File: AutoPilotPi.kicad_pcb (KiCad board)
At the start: 4 copper layers, 32.9 x 59.2 mm, 120 parts, among them J1 Conn_01x04_MountingPin, J2 Conn_01x03, J3 Conn_01x02, J4 USB_C_Receptacle, J5 Conn_01x03, J6 Conn_01x03, J7 Conn_01x03, M1 xr819, M2 mini_elrs, Q1 Q_NMOS_GSD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

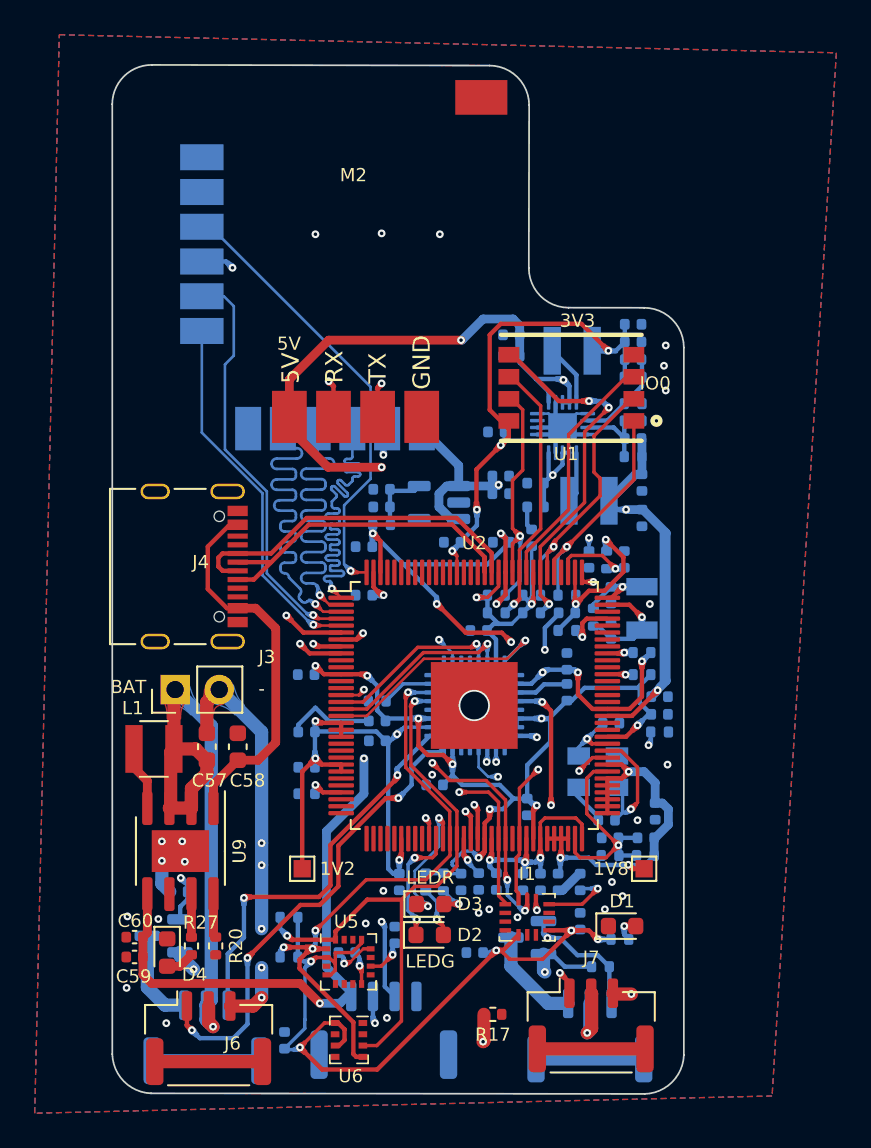
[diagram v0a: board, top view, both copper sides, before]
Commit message: add esp32 as wifi card
Signed-off-by: huangzzk <huangcmzzk@gmail.com>
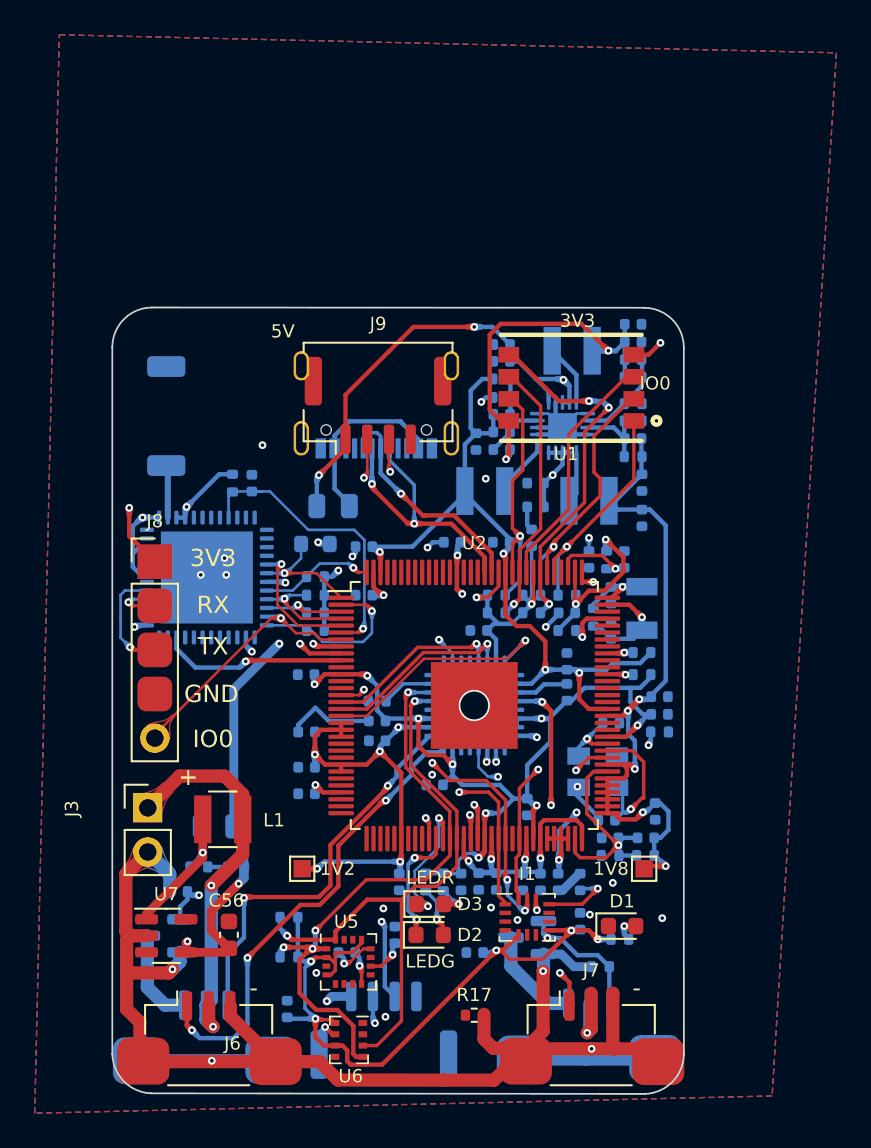
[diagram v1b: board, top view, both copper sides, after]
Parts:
- removed C59: 1u, Capacitor_SMD:C_0402_1005Metric
- removed C60: 0.1u, Capacitor_SMD:C_0402_1005Metric
- removed M1: xr819, ic_footprint:xr819_module
- removed M2: mini_elrs, ic_footprint:mini_elrs
- removed U9: ETA9640, Package_SO:SOIC-8-1EP_3.9x4.9mm_P1.27mm_EP2.41x3.3mm
- added AE1: Antenna, RF_Antenna:Johanson_2450AT43F0100, B.Cu at (74.7, 52.4)
- added D5: D, Diode_SMD:D_0805_2012Metric, B.Cu at (84.3, 57.6)
- added J8: Conn_01x05, Connector_PinHeader_2.54mm:PinHeader_1x05_P2.54mm_Vertical, F.Cu at (74.1, 60.8)
- added J9: Conn_01x04_MountingPin, Connector_Molex:Molex_CLIK-Mate_502382-0470_1x04-1MP_P1.25mm_Vertical, F.Cu at (86.9, 51.8)
- added L4: 2.2uH, Inductor_SMD:L_Abracon_ASPI-3012S, B.Cu at (93.1, 56.7)
- added R30: 10K, Resistor_SMD:R_0402_1005Metric, B.Cu at (83.3, 63.8)
- added R31: 10K, Resistor_SMD:R_0402_1005Metric, B.Cu at (83.3, 64.8)
- added R32: NC, Resistor_SMD:R_0603_1608Metric, B.Cu at (83.3, 59.8)
- added R33: 10K, Resistor_SMD:R_0402_1005Metric, B.Cu at (83.3, 61.7)
- added R34: 10K, Resistor_SMD:R_0402_1005Metric, B.Cu at (83.3, 62.7)
- added R35: 5R, Resistor_SMD:R_0402_1005Metric, B.Cu at (76.6, 78.4)
- added U7: TPS613222ADBV, Package_TO_SOT_SMD:SOT-23-5, F.Cu at (74.7, 82.3)
- C34: value 4.7u -> 0.1u
- C38: value 0.1u -> 220p
- C56: value 0.1u -> 22uF; footprint Capacitor_SMD:C_0402_1005Metric -> Capacitor_SMD:C_0603_1608Metric; moved to F.Cu
- C57: value 10u -> 0.1uF; footprint Capacitor_SMD:C_0603_1608Metric -> Capacitor_SMD:C_0402_1005Metric; moved to B.Cu
- C58: value 10u -> 220p; footprint Capacitor_SMD:C_0603_1608Metric -> Capacitor_SMD:C_0402_1005Metric; moved to B.Cu
- D4: value LED -> D; footprint LED_SMD:LED_0603_1608Metric -> Diode_SMD:D_0805_2012Metric; moved to B.Cu
- J2, J5, J6, J7: value Conn_01x03 -> Conn_01x03_MountingPin
- J4, R27: moved to B.Cu
- L1: value L -> 2.2uH
- R14: value 0R -> 100k
- R20: value 1.2k -> 100K; moved to B.Cu
- R21: value 0R -> NC
- U8: value ME6212C12M5G -> ESP32-PICO-D4; footprint Package_TO_SOT_SMD:SOT-23-5 -> Package_DFN_QFN:QFN-48-1EP_7x7mm_P0.5mm_EP5.3x5.3mm
- moved R20 36.6 mm to (94.0, 50.3), turned to 0 degrees
- moved C56 29.8 mm to (78.3, 82.3), turned to 90 degrees
- moved R27 26.7 mm to (78.5, 56.3), turned to -90 degrees
- moved C57 15.4 mm to (79.7, 56.3)
- moved U8 14.0 mm to (77.1, 61.7), turned to -90 degrees
- moved J4 14.0 mm to (86.8, 51.8), turned to 0 degrees
- moved R14 10.1 mm to (94.0, 51.4), turned to 0 degrees
- moved C38 8.15 mm to (94.0, 52.3), turned to 0 degrees
- moved D4 7.82 mm to (77.7, 76.0), turned to 180 degrees
- moved J3 6.99 mm to (73.7, 75.0), turned to 0 degrees
- moved C58 6.92 mm to (78.7, 78.4), turned to 0 degrees
- moved C34 6.61 mm to (92.6, 53.9), turned to -90 degrees
- moved L1 5.67 mm to (78.0, 75.6)
- moved C31 2.54 mm to (94.0, 53.3)
- moved C52 1.81 mm to (81.7, 86.6)
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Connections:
- C31 pad 1: +1V8 -> +1V2
- C34 pad 1: Net-(C34-Pad1) -> +1V2
- C38 pad 1: Net-(C34-Pad1) -> +1V2
- C38 pad 2: GND -> Net-(C38-Pad2)
- C56 pad 1: +1V8 -> +5V
- C57 pad 1: +BATT -> /WENABLE
- C57 pad 2: GNDPWR -> GND
- C58 pad 1: GND -> Net-(C58-Pad1)
- C58 pad 2: VBUS -> +5V
- D4 pad 1: GND -> +5V
- J2 pad MP: (no net) -> GNDPWR
- J5 pad MP: (no net) -> GNDPWR
- J6 pad MP: (no net) -> GNDPWR
- J7 pad MP: (no net) -> GNDPWR
- L1 pad 2: Net-(L1-Pad2) -> Net-(D4-Pad2)
- R14 pad 1: Net-(C34-Pad1) -> GND
- R14 pad 2: +1V2 -> Net-(C38-Pad2)
- R20 pad 1: Net-(R20-Pad1) -> +1V2
- R20 pad 2: GND -> Net-(C38-Pad2)
- R27 pad 1: Net-(D4-Pad2) -> +3V3
- R27 pad 2: Net-(R27-Pad2) -> /WENABLE
- U2 pad 10: unconnected-(U2-Pad10) -> /WREST2
- U2 pad 6: /WIRQ -> /WENABLE
- U3 pad 11: unconnected-(U3-Pad11) -> Net-(L4-Pad2)
- U3 pad 14: unconnected-(U3-Pad14) -> Net-(C38-Pad2)
- U3 pad 9: GND -> +5V
- U8 pad 1: +1V8 -> +3V3
- U8 pad 2: GND -> /esp32_wifi/ESP32_ANT
- U8 pad 3: +1V8 -> +3V3
- U8 pad 4: unconnected-(U8-Pad4) -> +3V3
- U8 pad 5: Net-(C34-Pad1) -> unconnected-(U8-Pad5)
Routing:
- net +1V8: track 87.0 -> 51.0 mm, vias 6 -> 7
- net /WIRQ: track 26.8 -> 0.00 mm, vias 2 -> 0
- net (no net): track 24.8 -> 0.00 mm
- net /SD1_D3: track 25.9 -> 6.60 mm
- net /SD1_D0: track 24.2 -> 5.28 mm
- net /SD1_CMD: track 24.0 -> 6.24 mm
- net /SD1_D2: track 24.8 -> 7.00 mm
- net /WENABLE: track 0.00 -> 17.5 mm, vias 0 -> 1
- net +BATT: track 65.9 -> 49.8 mm, vias 2 -> 3
- net /SD1_D1: track 25.6 -> 9.88 mm
- net /SD1_CLK: track 21.2 -> 7.46 mm
- net +5V: track 96.3 -> 83.4 mm, vias 6 -> 8
- net VBUS: track 22.0 -> 10.4 mm
- net /WREST2: track 0.00 -> 10.7 mm, vias 0 -> 1
- net +3V3: track 203.9 -> 193.3 mm, vias 25 -> 32
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- added copper zone on In2.Cu, net +3V3
- added copper zone on In1.Cu, net GND
- removed copper zone on In1.Cu, net +3V3
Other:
- board size 32.9 x 59.2 mm -> 32.9 x 45.3 mm
- board text added: "+"
- board text added: "GND"
- board text removed: "BAT"
